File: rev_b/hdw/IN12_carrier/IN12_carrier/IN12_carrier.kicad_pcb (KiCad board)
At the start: 4 copper layers, 200 x 50 mm, 200 parts, among them J1001 Cap SNS, J201 Conn_02x32_Top_Bottom, Q401 MMSTA42, Q402 MMSTA42, Q403 MMSTA42, Q404 MMSTA92, Q405 MMSTA92, Q406 MMSTA92, Q407 MMSTA42, Q408 MMSTA42, Q409 MMSTA42, Q410 MMSTA92, Q411 MMSTA92, Q412 MMSTA92, Q501 MMSTA42, Q502 MMSTA42, Q503 MMSTA42, Q504 MMSTA42, Q505 MMSTA42, Q506 MMSTA42, Q507 MMSTA42, Q508 MMSTA42, Q509 MMSTA42, Q510 MMSTA42, Q511 MMSTA42, Q512 MMSTA42, Q513 MMSTA42, Q514 MMSTA42, Q515 MMSTA42, U1001 TCA9555RGER, U1002 24AA02-OT, U1003 AT42QT1010-TSHR, U1004 AT42QT1010-TSHR, U1005 AT42QT1010-TSHR, U1006 AT42QT1010-TSHR, U1007 AT42QT1010-TSHR, U301 DS1683, U302 LTC4316DD, U701 LP5009, U702 LP5009, U703 LP5009

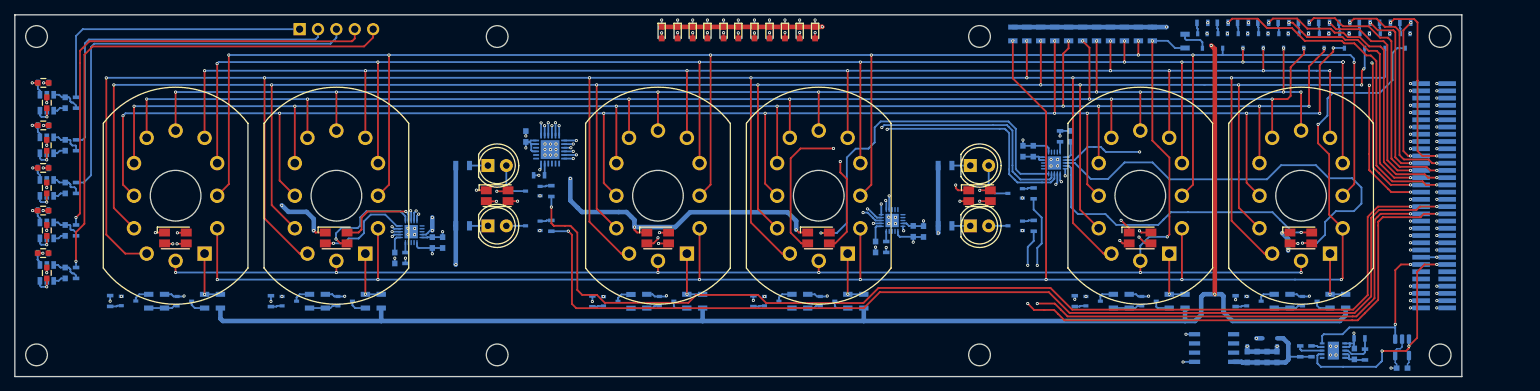
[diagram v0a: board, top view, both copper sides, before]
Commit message: got IN12 carrier board unconnects to 0
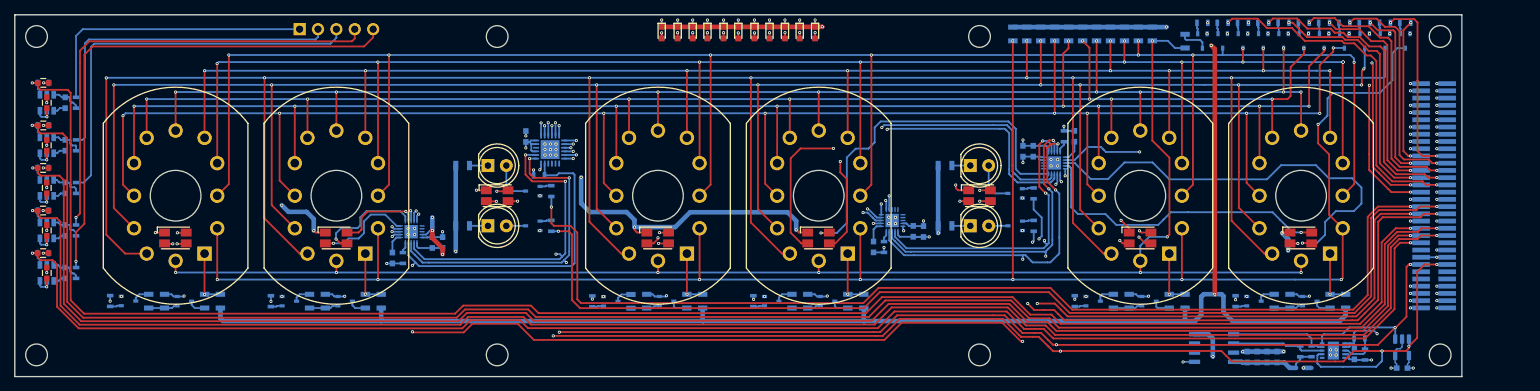
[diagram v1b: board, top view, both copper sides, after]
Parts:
- moved D301 6.20 mm to (213.4, 131.1), turned to 0 degrees
- moved R704 0.53 mm to (180.3, 99.1)
- moved C701 0.51 mm to (181.7, 99.1)
- moved R705 0.36 mm to (88.9, 116.0)
- moved C702 0.33 mm to (87.5, 116.0)
- moved R706 0.30 mm to (155.4, 114.4)
- moved C703 0.28 mm to (153.9, 114.4)
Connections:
- J201 pad 27: USB_UART_RX -> unconnected-(J201-Pin_27-Pad27)
- J201 pad 59: USB_UART_TX -> unconnected-(J201-Pin_59-Pad59)
- U701 pad 17: I2C_SDA -> I2C_DSP_SDA
- U701 pad 18: I2C_SCL -> I2C_DSP_SCL
- U702 pad 17: I2C_SDA -> I2C_DSP_SDA
- U702 pad 18: I2C_SCL -> I2C_DSP_SCL
- U703 pad 17: I2C_SDA -> I2C_DSP_SDA
- U703 pad 18: I2C_SCL -> I2C_DSP_SCL
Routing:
- net Pushbutton_Power: track 4.76 -> 238.5 mm
- net Pushbutton_Left: track 4.76 -> 236.8 mm
- net I2C_DSP_SDA: track 33.1 -> 264.2 mm, vias 3 -> 11
- net I2C_DSP_SCL: track 25.0 -> 252.9 mm, vias 2 -> 10
- net Pushbutton_Right: track 4.59 -> 227.3 mm
- net Pushbutton_Up: track 4.62 -> 225.7 mm
- net Pushbutton_Down: track 4.66 -> 216.3 mm
- net Tube_LED_Enable: track 1.63 -> 198.0 mm, vias 0 -> 6
- net Net-(U301-SCL): track 1.53 -> 13.6 mm
- net GND: track 102.1 -> 113.5 mm
- net Net-(U301-SDA): track 3.57 -> 12.9 mm
- net +3.3V: track 120.4 -> 126.7 mm, vias 30 -> 32
- net Net-(D301-K): track 15.0 -> 12.3 mm
- net Cathode_0: track 268.7 -> 266.8 mm
- net unconnected-(J201-Pin_56-Pad56): track 1.43 -> 0.00 mm, vias 1 -> 0
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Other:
- board text added: "To-Do: * Fix via sizes/annular ring design rule * Enter stackup in design rules * Stackup legend * Owl * Board name * Board date * Board stats"
- board text removed: "To-Do: * Fix I2C net naming * Enter stackup in design rules * Stackup legend * Owl * Board name * Board date * Board stats"

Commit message: added BOM for IN12 carrier, finished routing, some schematic tweaks, adjusted design rules for ERC
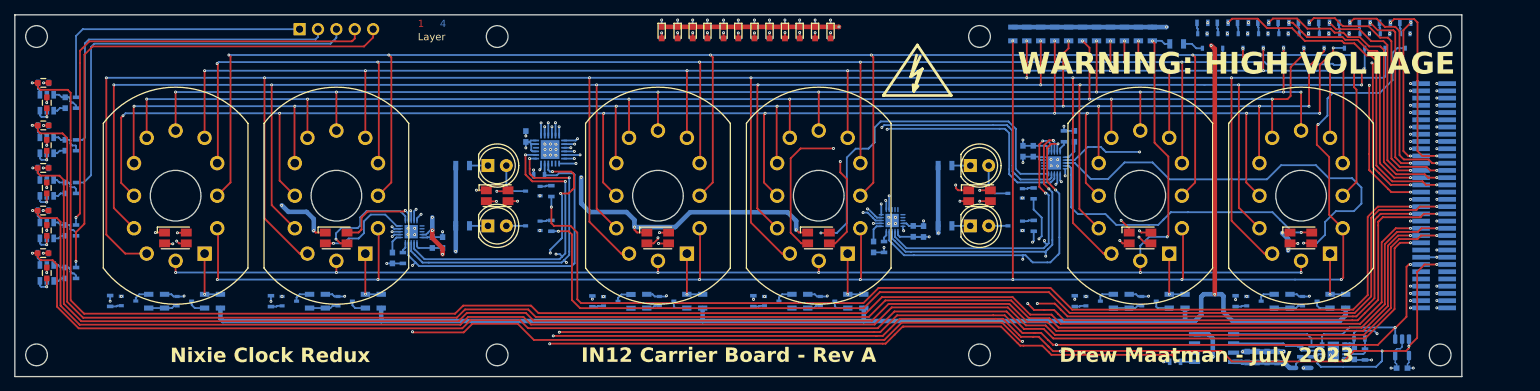
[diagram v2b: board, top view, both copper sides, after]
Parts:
- added D901: Orange, LEDs:LED_0603, F.Cu at (148.0, 84.8)
- added G***: Owl_1_Logo, Custom Footprints Library:Owl_1_Logo, B.Cu at (94.9, 95.4)
- added R305: 10k, Resistors_SMD:R_0603, B.Cu at (195.6, 130.3)
- added R901: 499, Resistors_SMD:R_0603, B.Cu at (148.0, 84.8)
- added REF**: Symbol_HighVoltage_Type2_Silkscreen_VerySmall, Custom Footprints Library:Symbol_HighVoltage_Type2_Silkscreen_VerySmall, F.Cu at (160.0, 90.7)
- added REF**: Symbol_HighVoltage_Type2_Silkscreen_VerySmall, Custom Footprints Library:Symbol_HighVoltage_Type2_Silkscreen_VerySmall, B.Cu at (222.1, 93.1)
- moved R514 1.22 mm to (195.8, 86.4), turned to 180 degrees
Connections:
- U1001 pad 13: unconnected-(U1001-P13-Pad13) -> Set_Color_LED
- U1001 pad 16: unconnected-(U1001-P16-Pad16) -> Tube_ETC_Enable
- U301 pad 1: +3.3V -> Tube_ETC_Enable
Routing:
- net Tube_ETC_Enable: track 0.00 -> 122.8 mm, vias 0 -> 5
- net Set_Color_LED: track 0.00 -> 54.3 mm, vias 0 -> 2
- net +3.3V: track 126.7 -> 147.7 mm, vias 32 -> 31
- net GND: track 113.5 -> 116.7 mm, vias 90 -> 91
- net Cathode_DP: track 204.7 -> 202.2 mm
- net Net-(D901-A): track 0.00 -> 1.55 mm, vias 0 -> 1
- net Cathode_9: track 278.7 -> 280.1 mm
- net Net-(Q511-C): track 4.05 -> 2.86 mm
- net Cathode_8: track 244.2 -> 244.9 mm
- net Cathode_0: track 266.8 -> 267.4 mm
- net Cathode_3: track 259.3 -> 259.9 mm
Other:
- board text added: "0"
- board text added: "0 mm"
- board text added: "0.01 mm"
- board text added: "0.0152 mm"
- board text added: "0.02"
- board text added: "0.035 mm"
- board text added: "0.2104 mm"
- board text added: "1"
- board text added: "1.065 mm"
- board text added: "2"
- board text added: "3"
- board text added: "3.3"
- board text added: "4"
- board text added: "4.6"
- board text added: "B.Cu"
- board text added: "B.Mask"
- board text added: "B.Paste"
- board text added: "B.Silkscreen"
- board text added: "Bottom Silk Screen"
- board text added: "Bottom Solder Mask"
- board text added: "Bottom Solder Paste"
- board text added: "Color"
- board text added: "Dielectric 1"
- board text added: "Dielectric 2"
- board text added: "Dielectric 3"
- board text added: "Drew Maatman - July 2023"
- board text added: "Epsilon R"
- board text added: "F.Cu"
- board text added: "F.Mask"
- board text added: "F.Paste"
- board text added: "F.Silkscreen"
- board text added: "FR4"
- board text added: "IN12 Carrier Board - Rev A"
- board text added: "In1.Cu"
- board text added: "In2.Cu"
- board text added: "JLC 4 Layer No Requirement Stackup"
- board text added: "Layer"
- board text added: "Layer Name"
- board text added: "Loss Tangent"
- board text added: "Material"
- board text added: "Nixie Clock Redux"
- board text added: "Nixie Clock Redux IN12 Carrier Rev A: Pads: 724 Vias: 414 Track Segments: 2425 Nets: 199 Components: 249"
- board text added: "Not specified"
- board text added: "Power Left Right Up Down"
- board text added: "Thickness (mm)"
- board text added: "Top Silk Screen"
- board text added: "Top Solder Mask"
- board text added: "Top Solder Paste"
- board text added: "Type"
- board text added: "WARNING: HIGH VOLTAGE"
- board text added: "copper"
- board text added: "core"
- board text added: "prepreg"
- board text removed: "To-Do: * Fix via sizes/annular ring design rule * Enter stackup in design rules * Stackup legend * Owl * Board name * Board date * Board stats"

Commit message: lots of PCB improvements/touch ups
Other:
- board text added: "JLCJLCJLCJLC"
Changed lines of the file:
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@@
   (gr_text "WARNING: HIGH VOLTAGE" (at 215.265 92.583) (layer "B.SilkS")
     (effects (font (face "Courier New") (size 3 3) (thickness 0.4) bold) (justify left mirror))
-    (render_cache "WARNING: HIGH VOLTAGE" -0
+    (render_cache "WARNING: HIGH VOLTAGE" 0
       (polygon
         (pts
@@
     )
   )
+  (gr_text "JLCJLCJLCJLC" (at 48.641 84.4296) (layer "F.SilkS")
+    (effects (font (size 1 1) (thickness 0.15)) (justify left))
+  )
   (gr_text "WARNING: HIGH VOLTAGE" (at 173.863 89.0778) (layer "F.SilkS")

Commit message: added user5 layer to IN12 carrier layout for acrylic panel
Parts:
- added ?: , clipboard:0f9a564b-2544-4a1f-a798-1a23f2962fef, F.Cu at (213.0, 107.3)
- added ?: , clipboard:0f9a564b-2544-4a1f-a798-1a23f2962fef, F.Cu at (124.2, 107.3)
- added ?: , clipboard:0f9a564b-2544-4a1f-a798-1a23f2962fef, F.Cu at (79.7, 107.3)
- added ?: , clipboard:0f9a564b-2544-4a1f-a798-1a23f2962fef, F.Cu at (57.5, 107.3)
- added ?: , clipboard:0f9a564b-2544-4a1f-a798-1a23f2962fef, F.Cu at (146.4, 107.3)
- added ?: , clipboard:0f9a564b-2544-4a1f-a798-1a23f2962fef, F.Cu at (190.8, 107.3)
